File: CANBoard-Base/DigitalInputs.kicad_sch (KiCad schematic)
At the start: 11 parts, among them U4 SRV05-4

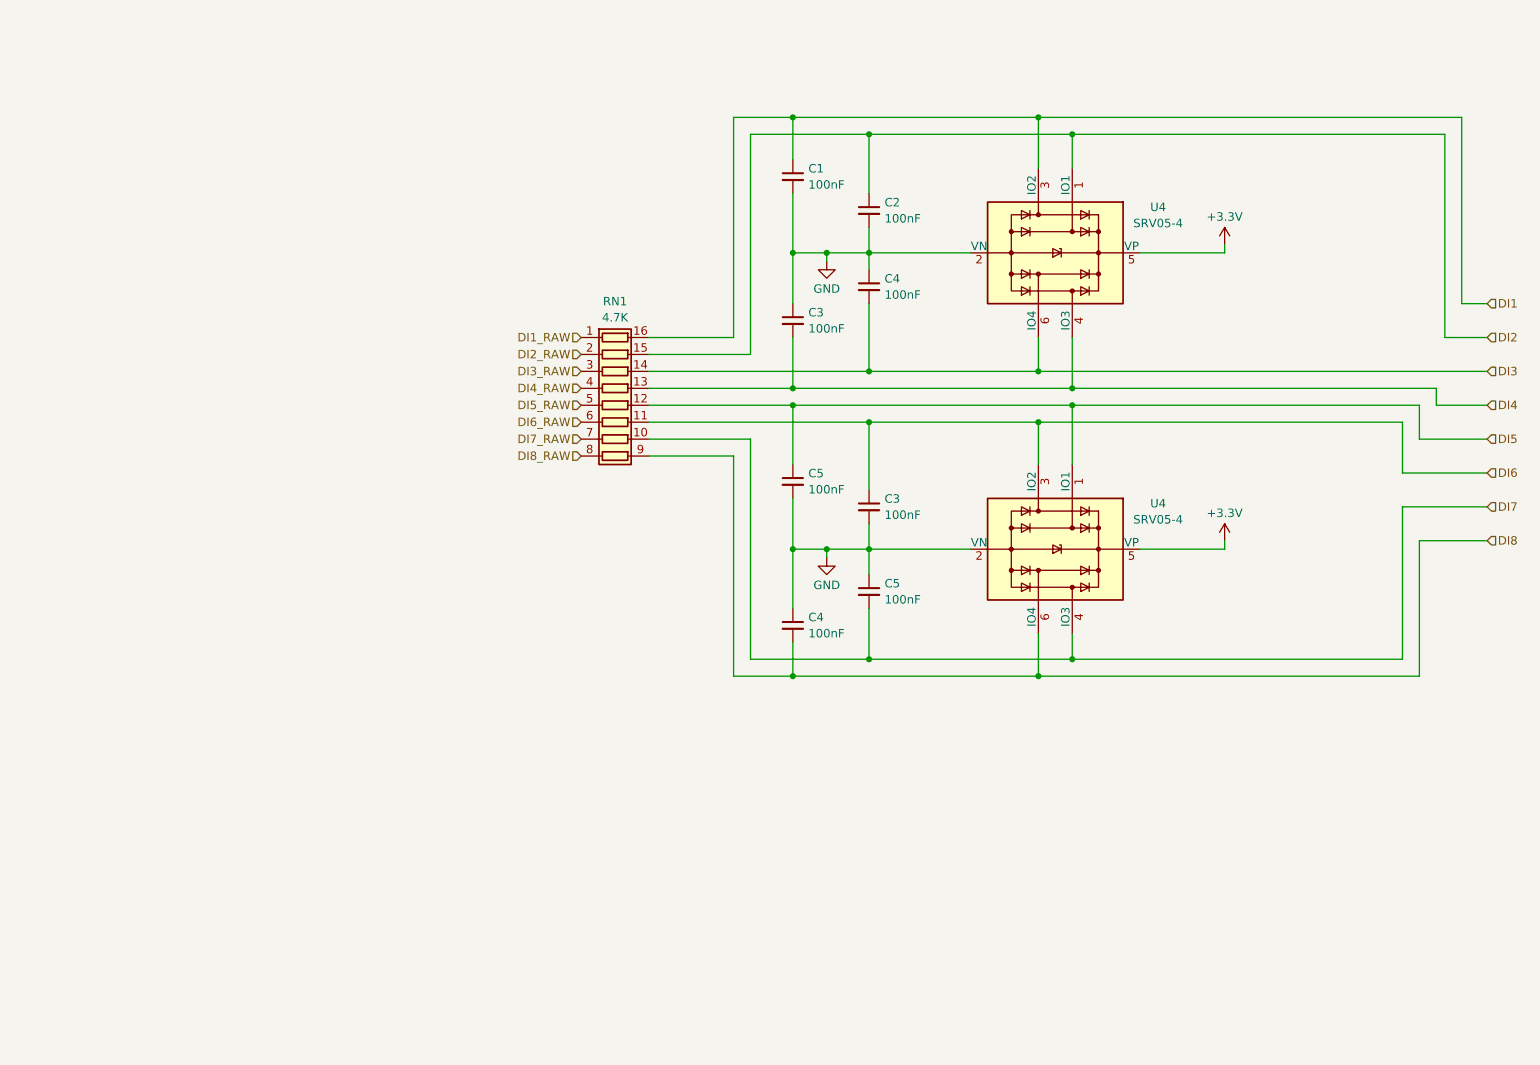
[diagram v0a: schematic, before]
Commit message: Switched to v2
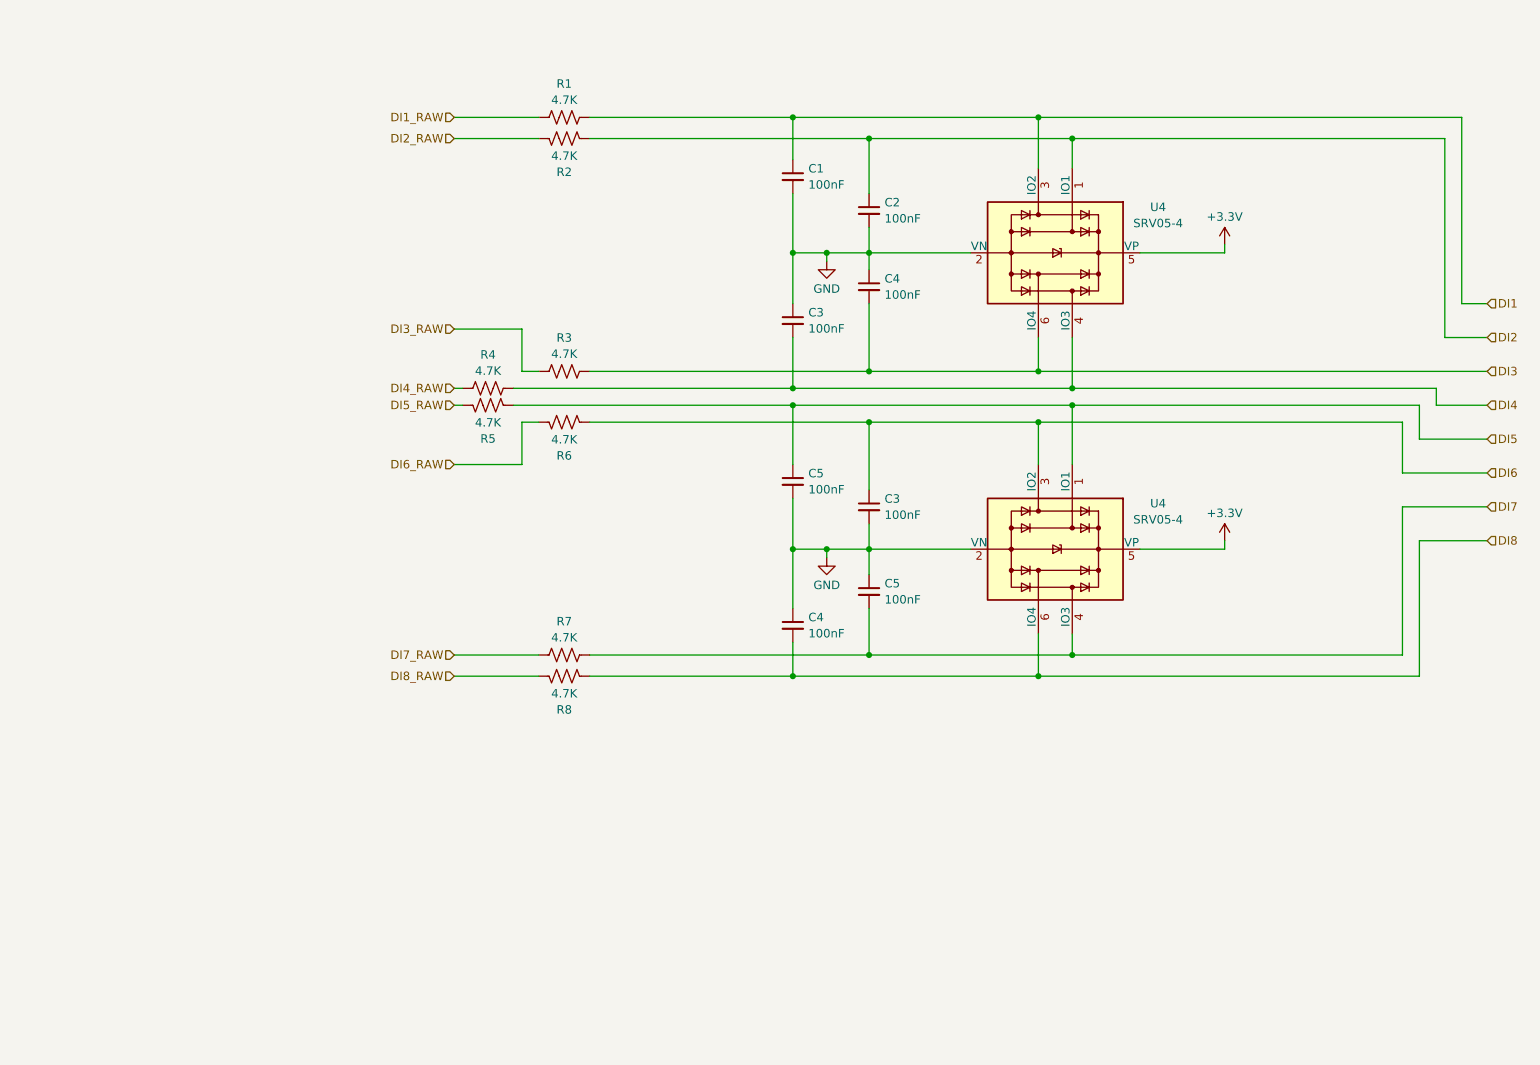
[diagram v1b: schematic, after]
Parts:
- removed RN1: 4.7K, symbol Device:R_Pack08
- added R1, R2, R3, R4, R5, R6, R7, R8: 4.7K, Resistor_SMD:R_0805_2012Metric, symbol Device:R_US
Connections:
- net DI1: now also R1.2
- net DI1_RAW: now also R1.1
- net DI2: now also R2.2
- net DI2_RAW: now also R2.1
- net DI3: now also R3.2
- net DI3_RAW: now also R3.1
- net DI4: now also R4.2
- net DI4_RAW: now also R4.1
- net DI5: now also R5.2
- net DI5_RAW: now also R5.1
- net DI6: now also R6.2
- net DI6_RAW: now also R6.1
- net DI7: now also R7.2
- net DI7_RAW: now also R7.1
- net DI8: now also R8.2
- net DI8_RAW: now also R8.1

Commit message: Update to Kicad 8
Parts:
- renumbered C5 to C10, C3 to C11, C4 to C12, C5 to C13, C1 to C6, C2 to C7, C3 to C8, C4 to C9, U4 to U6, U4 to U7

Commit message: first layout complete
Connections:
- net DI5: now also U6.3 (IO2); no longer U6.1 (IO1)
- net DI6: now also U6.1 (IO1); no longer U6.3 (IO2)
- net DI7: now also U6.6 (IO4); no longer U6.4 (IO3)
- net DI8: now also U6.4 (IO3); no longer U6.6 (IO4)
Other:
- moved on the sheet: R7
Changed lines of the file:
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@@
-	)
-	(junction
-		(at 182.88 127)
-		(diameter 0)
-		(color 0 0 0 0)
 	)
 	(junction
@@
 	)
 	(junction
+		(at 187.96 88.9)
+		(diameter 0)
+		(color 0 0 0 0)
+	)
+	(junction
 		(at 146.05 43.18)
 		(diameter 0)
@@
 	)
 	(junction
-		(at 187.96 86.36)
-		(diameter 0)
-		(color 0 0 0 0)
-	)
-	(junction
-		(at 187.96 123.825)
-		(diameter 0)
-		(color 0 0 0 0)
-	)
-	(junction
-		(at 182.88 88.9)
+		(at 157.48 123.19)
+		(diameter 0)
+		(color 0 0 0 0)
+	)
+	(junction
+		(at 182.88 86.36)
+		(diameter 0)
+		(color 0 0 0 0)
+	)
+	(junction
+		(at 187.96 127)
+		(diameter 0)
+		(color 0 0 0 0)
+	)
+	(junction
+		(at 182.88 123.19)
 		(diameter 0)
 		(color 0 0 0 0)
@@
 	)
 	(junction
-		(at 157.48 123.825)
-		(diameter 0)
-		(color 0 0 0 0)
-	)
-	(junction
 		(at 146.05 63.5)
 		(diameter 0)
@@
 	(wire
 		(pts
+			(xy 187.96 120.65) (xy 187.96 127)
+		)
+		(stroke
+			(width 0)
+			(type default)
+		)
+	)
+	(wire
+		(pts
 			(xy 146.05 107.95) (xy 146.05 116.84)
 		)
@@
 	(wire
 		(pts
-			(xy 157.48 116.84) (xy 157.48 123.825)
+			(xy 157.48 116.84) (xy 157.48 123.19)
 		)
 		(stroke
@@
 	(wire
 		(pts
-			(xy 187.96 123.825) (xy 237.49 123.825)
+			(xy 95.25 123.19) (xy 107.95 123.19)
 		)
 		(stroke
@@
 	(wire
 		(pts
-			(xy 95.25 123.825) (xy 107.95 123.825)
-		)
-		(stroke
-			(width 0)
-			(type default)
-		)
-	)
-	(wire
-		(pts
 			(xy 246.38 43.18) (xy 182.88 43.18)
 		)
@@
 	(wire
 		(pts
-			(xy 237.49 123.825) (xy 237.49 101.6)
-		)
-		(stroke
-			(width 0)
-			(type default)
-		)
-	)
-	(wire
-		(pts
-			(xy 187.96 120.65) (xy 187.96 123.825)
+			(xy 237.49 123.19) (xy 237.49 101.6)
 		)
 		(stroke
@@
 	(wire
 		(pts
-			(xy 146.05 127) (xy 182.88 127)
+			(xy 146.05 127) (xy 187.96 127)
 		)
 		(stroke
@@
 	(wire
 		(pts
-			(xy 187.96 86.36) (xy 187.96 95.25)
-		)
-		(stroke
-			(width 0)
-			(type default)
-		)
-	)
-	(wire
-		(pts
-			(xy 146.05 86.36) (xy 187.96 86.36)
+			(xy 146.05 86.36) (xy 182.88 86.36)
 		)
 		(stroke
@@
 	(wire
 		(pts
-			(xy 157.48 88.9) (xy 182.88 88.9)
+			(xy 157.48 88.9) (xy 187.96 88.9)
 		)
 		(stroke
@@
 	(wire
 		(pts
-			(xy 182.88 120.65) (xy 182.88 127)
-		)
-		(stroke
-			(width 0)
-			(type default)
-		)
-	)
-	(wire
-		(pts
 			(xy 95.25 46.355) (xy 107.95 46.355)
 		)
@@
 	(wire
 		(pts
-			(xy 115.57 123.825) (xy 157.48 123.825)
-		)
-		(stroke
-			(width 0)
-			(type default)
-		)
-	)
-	(wire
-		(pts
-			(xy 157.48 123.825) (xy 187.96 123.825)
+			(xy 115.57 123.19) (xy 157.48 123.19)
+		)
+		(stroke
+			(width 0)
+			(type default)
+		)
+	)
+	(wire
+		(pts
+			(xy 187.96 88.9) (xy 237.49 88.9)
+		)
+		(stroke
+			(width 0)
+			(type default)
+		)
+	)
+	(wire
+		(pts
+			(xy 157.48 123.19) (xy 182.88 123.19)
 		)
 		(stroke
@@
 	(wire
 		(pts
-			(xy 182.88 88.9) (xy 182.88 95.25)
-		)
-		(stroke
-			(width 0)
-			(type default)
-		)
-	)
-	(wire
-		(pts
 			(xy 151.13 63.5) (xy 151.13 64.77)
 		)
@@
 	(wire
 		(pts
+			(xy 187.96 127) (xy 240.03 127)
+		)
+		(stroke
+			(width 0)
+			(type default)
+		)
+	)
+	(wire
+		(pts
 			(xy 240.03 106.68) (xy 250.19 106.68)
 		)
@@
 	(wire
 		(pts
+			(xy 182.88 86.36) (xy 182.88 95.25)
+		)
+		(stroke
+			(width 0)
+			(type default)
+		)
+	)
+	(wire
+		(pts
 			(xy 146.05 54.61) (xy 146.05 63.5)
 		)
@@
 	(wire
 		(pts
+			(xy 182.88 120.65) (xy 182.88 123.19)
+		)
+		(stroke
+			(width 0)
+			(type default)
+		)
+	)
+	(wire
+		(pts
 			(xy 157.48 88.9) (xy 157.48 99.06)
 		)
@@
 	(wire
 		(pts
-			(xy 182.88 88.9) (xy 237.49 88.9)
-		)
-		(stroke
-			(width 0)
-			(type default)
-		)
-	)
-	(wire
-		(pts
 			(xy 237.49 88.9) (xy 237.49 96.52)
 		)
@@
 	(wire
 		(pts
-			(xy 187.96 86.36) (xy 240.03 86.36)
+			(xy 182.88 86.36) (xy 240.03 86.36)
 		)
 		(stroke
@@
 	(wire
 		(pts
-			(xy 182.88 127) (xy 240.03 127)
-		)
-		(stroke
-			(width 0)
-			(type default)
-		)
-	)
-	(wire
-		(pts
 			(xy 187.96 76.2) (xy 187.96 83.82)
 		)
@@
 	(wire
 		(pts
+			(xy 182.88 123.19) (xy 237.49 123.19)
+		)
+		(stroke
+			(width 0)
+			(type default)
+		)
+	)
+	(wire
+		(pts
+			(xy 187.96 88.9) (xy 187.96 95.25)
+		)
+		(stroke
+			(width 0)
+			(type default)
+		)
+	)
+	(wire
+		(pts
 			(xy 242.57 86.36) (xy 242.57 83.82)
 		)
@@
 	(hierarchical_label "DI7_RAW"
 		(shape input)
-		(at 95.25 123.825 180)
+		(at 95.25 123.19 180)
 		(fields_autoplaced yes)
 		(effects
@@
 	(symbol
 		(lib_id "Device:R_US")
-		(at 111.76 123.825 90)
+		(at 111.76 123.19 90)
 		(unit 1)
 		(exclude_from_sim no)
@@
 		(fields_autoplaced yes)
 		(property "Reference" "R7"
-			(at 111.76 118.7917 90)
+			(at 111.76 118.1567 90)
 			(effects
 				(font
@@
 		)
 		(property "Value" "4.7K"
-			(at 111.76 121.2159 90)
+			(at 111.76 120.5809 90)
 			(effects
 				(font
@@
 		)
 		(property "Footprint" "Resistor_SMD:R_0805_2012Metric"
-			(at 112.014 122.809 90)
+			(at 112.014 122.174 90)
 			(effects
 				(font
@@
 		)
 		(property "Datasheet" "~"
-			(at 111.76 123.825 0)
+			(at 111.76 123.19 0)
 			(effects
 				(font
@@
 		)
 		(property "Description" ""
-			(at 111.76 123.825 0)
-			(effects
-				(font
+			(at 111.76 123.19 0)
+			(effects
+				(font

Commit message: as built v1
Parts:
- C10, C11, C12, C13, C6, C7, C8, C9: JLC_PN (none) -> C49678
- R1, R2, R3, R4, R5, R6, R7, R8: JLC_PN (none) -> C17673
- U6, U7: JLC_PN (none) -> C384887
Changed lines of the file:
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@@
+			)
+		)
+		(property "JLC_PN" "C384887"
+			(at 185.42 63.5 0)
+			(effects
+				(font
+					(size 1.27 1.27)
+				)
+				(hide yes)
 			)
 		)
@@
 			)
 		)
+		(property "JLC_PN" "C49678"
+			(at 146.05 73.66 0)
+			(effects
+				(font
+					(size 1.27 1.27)
+				)
+				(hide yes)
+			)
+		)
 		(pin "1"
 		)
@@
 			)
 		)
+		(property "JLC_PN" "C17673"
+			(at 111.76 123.19 0)
+			(effects
+				(font
+					(size 1.27 1.27)
+				)
+				(hide yes)
+			)
+		)
 		(pin "1"
 		)
@@
 			)
 		)
+		(property "JLC_PN" "C49678"
+			(at 157.48 101.6 0)
+			(effects
+				(font
+					(size 1.27 1.27)
+				)
+				(hide yes)
+			)
+		)
 		(pin "1"
 		)
@@
 			)
 		)
+		(property "JLC_PN" "C17673"
+			(at 100.33 83.82 0)
+			(effects
+				(font
+					(size 1.27 1.27)
+				)
+				(hide yes)
+			)
+		)
 		(pin "1"
 		)
@@
 			)
 		)
+		(property "JLC_PN" "C49678"
+			(at 146.05 52.07 0)
+			(effects
+				(font
+					(size 1.27 1.27)
+				)
+				(hide yes)
+			)
+		)
 		(pin "1"
 		)
@@
 			)
 		)
+		(property "JLC_PN" "C49678"
+			(at 157.48 57.15 0)
+			(effects
+				(font
+					(size 1.27 1.27)
+				)
+				(hide yes)
+			)
+		)
 		(pin "1"
 		)
@@
 		)
 		(property "Description" ""
+			(at 111.76 43.18 0)
+			(effects
+				(font
+					(size 1.27 1.27)
+				)
+				(hide yes)
+			)
+		)
+		(property "JLC_PN" "C17673"
 			(at 111.76 43.18 0)
 			(effects
@@
 			)
 		)
+		(property "JLC_PN" "C17673"
+			(at 100.33 86.36 0)
+			(effects
+				(font
+					(size 1.27 1.27)
+				)
+				(hide yes)
+			)
+		)
 		(pin "1"
 		)
@@
 			)
 		)
+		(property "JLC_PN" "C17673"
+			(at 111.76 127 0)
+			(effects
+				(font
+					(size 1.27 1.27)
+				)
+				(hide yes)
+			)
+		)
 		(pin "1"
 		)
@@
 			)
 		)
+		(property "JLC_PN" "C49678"
+			(at 157.48 68.58 0)
+			(effects
+				(font
+					(size 1.27 1.27)
+				)
+				(hide yes)
+			)
+		)
 		(pin "1"
 		)
@@
 		)
 		(property "Description" ""
+			(at 146.05 97.79 0)
+			(effects
+				(font
+					(size 1.27 1.27)
+				)
+				(hide yes)
+			)
+		)
+		(property "JLC_PN" "C49678"
 			(at 146.05 97.79 0)
 			(effects
@@
 			)
 		)
+		(property "JLC_PN" "C17673"
+			(at 111.76 46.355 0)
+			(effects
+				(font
+					(size 1.27 1.27)
+				)
+				(hide yes)
+			)
+		)
 		(pin "1"
 		)
@@
 			)
 		)
+		(property "JLC_PN" "C384887"
+			(at 185.42 107.95 0)
+			(effects
+				(font
+					(size 1.27 1.27)
+				)
+				(hide yes)
+			)
+		)
 		(pin "1"
 		)
@@
 			)
 		)
+		(property "JLC_PN" "C17673"
+			(at 111.76 81.28 0)
+			(effects
+				(font
+					(size 1.27 1.27)
+				)
+				(hide yes)
+			)
+		)
 		(pin "1"
 		)
@@
 			)
 		)
+		(property "JLC_PN" "C49678"
+			(at 146.05 119.38 0)
+			(effects
+				(font
+					(size 1.27 1.27)
+				)
+				(hide yes)
+			)
+		)
 		(pin "1"
 		)
@@
 		)
 		(property "Description" ""
+			(at 157.48 114.3 0)
+			(effects
+				(font
+					(size 1.27 1.27)
+				)
+				(hide yes)
+			)
+		)
+		(property "JLC_PN" "C49678"
 			(at 157.48 114.3 0)
 			(effects
@@
 			(at 111.76 88.9 0)
 			(effects
+				(font
+					(size 1.27 1.27)
+				)
+				(hide yes)
+			)
+		)
+		(property "JLC_PN" "C17673"
+			(at 111.76 88.9 0)
+			(effects
